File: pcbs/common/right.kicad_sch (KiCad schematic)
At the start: 88 parts

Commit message: upload of pcb
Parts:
- removed rC? (x2): 27p, Capacitor_SMD:C_0402_1005Metric, symbol Device:C_Small
- removed rC? (x9): 100n, Capacitor_SMD:C_0402_1005Metric, symbol Device:C_Small
- removed rC? (x3): 1u, Capacitor_SMD:C_0402_1005Metric, symbol Device:C_Small
- removed rC? (x2): 10u, Capacitor_SMD:C_0402_1005Metric, symbol Device:C_Small
- removed rD?: 1N4148WT, Diode_SMD:D_SOD-523, symbol Diode:1N4148WT
- removed rEXLED? (x2), rLED? (x21): YS-SK6812MINI-E, kbd_local:YS-SK6812MINI-E, symbol kbd_local:YS-SK6812MINI-E
- removed rEXSW? (x2): RotaryEncoder_Switch, kbd_local:keyswitch_cherrymx_hotswap_1u_rotary_encoder_ec12, symbol Device:RotaryEncoder_Switch
- removed rF?: BSMD0603-050-12V, Fuse:Fuse_0603_1608Metric, symbol Device:Fuse
- removed rJ?: TYPE-C-31-M-13C, kbd_local:TYPE-C-31-M-13C, symbol Connector:USB_C_Receptacle_USB2.0
- removed rJ?: Conn_01x03, Connector_PinHeader_2.54mm:PinHeader_1x03_P2.54mm_Vertical, symbol Connector_Generic:Conn_01x03
- removed rJP1: SolderJumper_2_Bridged, Jumper:SolderJumper-2_P1.3mm_Open_RoundedPad1.0x1.5mm, symbol Jumper:SolderJumper_2_Bridged
- removed rR? (x2): 5.1k, Resistor_SMD:R_0402_1005Metric, symbol Device:R_Small
- removed rR? (x2): 1k, Resistor_SMD:R_0402_1005Metric, symbol Device:R
- removed rR?: 10k, Resistor_SMD:R_0402_1005Metric, symbol Device:R
- removed rR? (x2): 27, Resistor_SMD:R_0402_1005Metric, symbol Device:R_Small
- removed rSMDSW? (x2): TS-1088R-02026, kbd_local:TS-1088R-02026, symbol Switch:SW_Push
- removed rU?: NCP1117LPST33T3G, Package_TO_SOT_SMD:SOT-223-3_TabPin2, symbol Regulator_Linear:NCP1117-3.3_SOT223
- removed rU?: TPD4E05U06DQAR, Package_SON:USON-10_2.5x1.0mm_P0.5mm, symbol Power_Protection:TPD4EUSB30
- removed rU?: W25Q128JVSIQ, Package_SO:SOIC-8_5.23x5.23mm_P1.27mm, symbol Memory_Flash:W25Q128JVS
- removed rU?: RP2040, Package_DFN_QFN:QFN-56-1EP_7x7mm_P0.4mm_EP3.2x3.2mm, symbol MCU_RaspberryPi:RP2040
- removed rY?: 12MHz 18pF, Crystal:Crystal_SMD_3225-4Pin_3.2x2.5mm, symbol Device:Crystal_GND24_Small
- removed rZD?: ESD5Z5V0C, Diode_SMD:D_SOD-523, symbol Diode:ESD5Zxx
- added D1, D2: WS2812B, LED_SMD:LED_WS2812B_PLCC4_5.0x5.0mm_P3.2mm, symbol LED:WS2812B
- added LED43, LED45, LED46, LED48, LED49, LED51, LED52, LED54, LED55, LED57, LED58, LED60, LED61, LED62, LED63: MX_SK6812MINI-E, PCM_marbastlib-mx:LED_MX_6028R, symbol PCM_marbastlib-mx:MX_SK6812MINI-E
- added LED44, LED47, LED50, LED53, LED56, LED59: MX_SK6812MINI-E, PCM_marbastlib-mx:LED_MX_6028R-ROT, symbol PCM_marbastlib-mx:MX_SK6812MINI-E
- added U1: rp2040, various:rp2040promicro, symbol PCM_marbastlib-promicroish:rp2040
- rSW? (x20): footprint kbd:keyswitch_cherrymx_hotswap_1u -> PCM_marbastlib-mx:SW_MX_HS_CPG151101S11_1u
- rSW?: footprint kbd:keyswitch_cherrymx_hotswap_1.5u -> PCM_marbastlib-mx:SW_MX_HS_CPG151101S11_1u
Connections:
- net +5VR: now also D1.1 (VDD), D2.1 (VDD), LED43.1 (VDD), LED44.1 (VDD), LED45.1 (VDD), LED46.1 (VDD), LED47.1 (VDD), LED48.1 (VDD), LED49.1 (VDD), LED50.1 (VDD), LED51.1 (VDD), LED52.1 (VDD), LED53.1 (VDD), LED54.1 (VDD), LED55.1 (VDD), LED56.1 (VDD), LED57.1 (VDD), LED58.1 (VDD), LED59.1 (VDD), LED60.1 (VDD), LED61.1 (VDD), LED62.1 (VDD), LED63.1 (VDD), U1.5v
- net GNDR: now also D1.3 (VSS), D2.3 (VSS), LED43.4 (VSS), LED44.4 (VSS), LED45.4 (VSS), LED46.4 (VSS), LED47.4 (VSS), LED48.4 (VSS), LED49.4 (VSS), LED50.4 (VSS), LED51.4 (VSS), LED52.4 (VSS), LED53.4 (VSS), LED54.4 (VSS), LED55.4 (VSS), LED56.4 (VSS), LED57.4 (VSS), LED58.4 (VSS), LED59.4 (VSS), LED60.4 (VSS), LED61.4 (VSS), LED62.4 (VSS), LED63.4 (VSS), U1.G (GND)
- net KEY1: now also U1.0 (GP0)
- net KEY10: now also U1.5 (GP5)
- net KEY11: now also U1.16 (GP16)
- net KEY12: now also U1.27 (GP27)
- net KEY13: now also U1.28 (GP28)
- net KEY14: now also U1.21 (GP21)
- net KEY15: now also U1.8 (GP8)
- net KEY16: now also U1.9 (GP9)
- net KEY17: now also U1.23 (GP23)
- net KEY18: now also U1.29 (GP29)
- net KEY19: now also U1.11 (GP11)
- net KEY2: now also U1.3 (GP3)
- net KEY20: now also U1.20 (GP20)
- net KEY21: now also U1.25 (GP25)
- net KEY3: now also U1.14 (GP14)
- net KEY4: now also U1.22 (GP22)
- net KEY5: now also U1.26 (GP26)
- net KEY6: now also U1.15 (GP15)
- net KEY7: now also U1.4 (GP4)
- net KEY8: now also U1.1 (GP1)
- net KEY9: now also U1.2 (GP2)
- net LED: now also D2.2 (DOUT), U1.10 (GP10)
- net RE1A: no longer rJ?.1 (Pin_1)
- net REB: no longer rJ?.2 (Pin_2)
- net RX: now also U1.13 (GP13)
- net TX: now also U1.12 (GP12)
- new net: LED58.2 (DOUT), LED59.3 (DIN)
- new net: LED55.2 (DOUT), LED58.3 (DIN)
- new net: D1.2 (DOUT), D2.4 (DIN)
- new net: D1.4 (DIN), LED43.3 (DIN)
- new net: LED53.3 (DIN), LED56.2 (DOUT)
- new net: LED56.3 (DIN), LED59.2 (DOUT)
- new net: LED54.2 (DOUT), LED57.3 (DIN)
- new net: LED51.2 (DOUT), LED54.3 (DIN)
- new net: LED50.3 (DIN), LED53.2 (DOUT)
- new net: LED52.2 (DOUT), LED55.3 (DIN)
- new net: LED61.2 (DOUT), LED62.3 (DIN)
- new net: LED60.2 (DOUT), LED61.3 (DIN)
- new net: LED48.2 (DOUT), LED51.3 (DIN)
- new net: LED45.2 (DOUT), LED48.3 (DIN)
- new net: LED57.2 (DOUT), LED60.3 (DIN)
- new net: LED62.2 (DOUT), LED63.3 (DIN)
- new net: LED47.3 (DIN), LED50.2 (DOUT)
- new net: LED43.2 (DOUT), LED46.3 (DIN)
- new net: LED44.3 (DIN), LED47.2 (DOUT)
- new net: LED49.2 (DOUT), LED52.3 (DIN)
- new net: LED44.2 (DOUT), LED45.3 (DIN)
- new net: LED46.2 (DOUT), LED49.3 (DIN)
- new net SCL: U1.7 (GP7), rJ?.2 (Pin_2)
- new net SDA: U1.6 (GP6), rJ?.1 (Pin_1)
- no-connect marks 3 -> 4
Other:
- note removed: "DEBUG"
- note removed: "Flash memory"
- note removed: "LEDs"
- note removed: "SPLIT_HAND_PIN"
- note removed: "USB ESD"
- note removed: "boot switch"
- note removed: "close to pin 44"
- note removed: "close to pin 45"

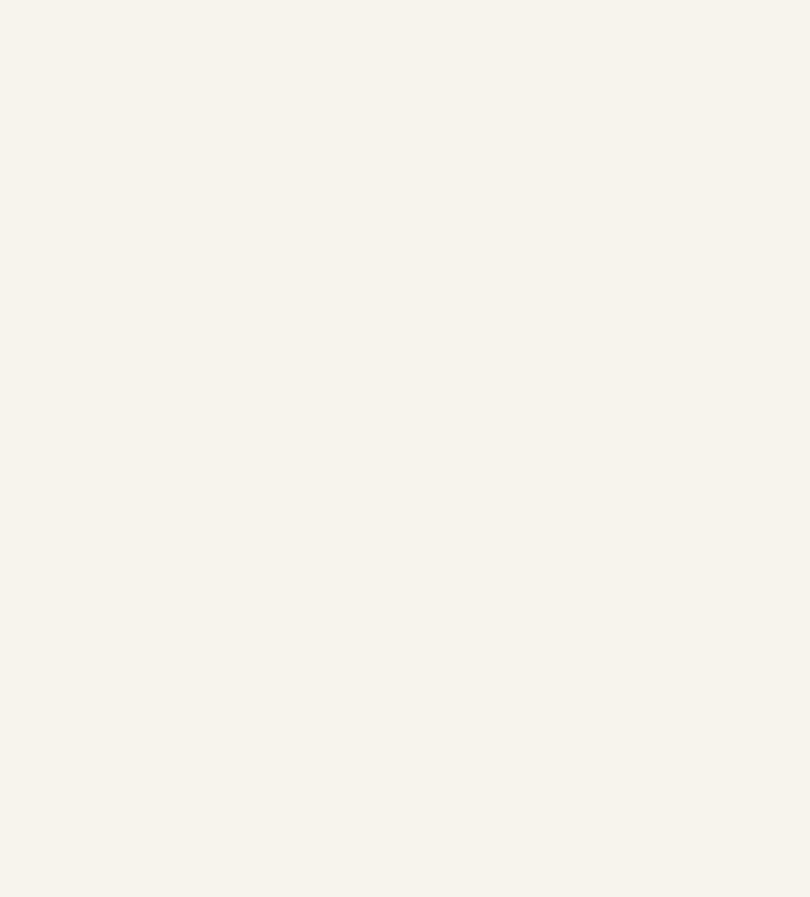
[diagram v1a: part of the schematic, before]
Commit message: split into left and right
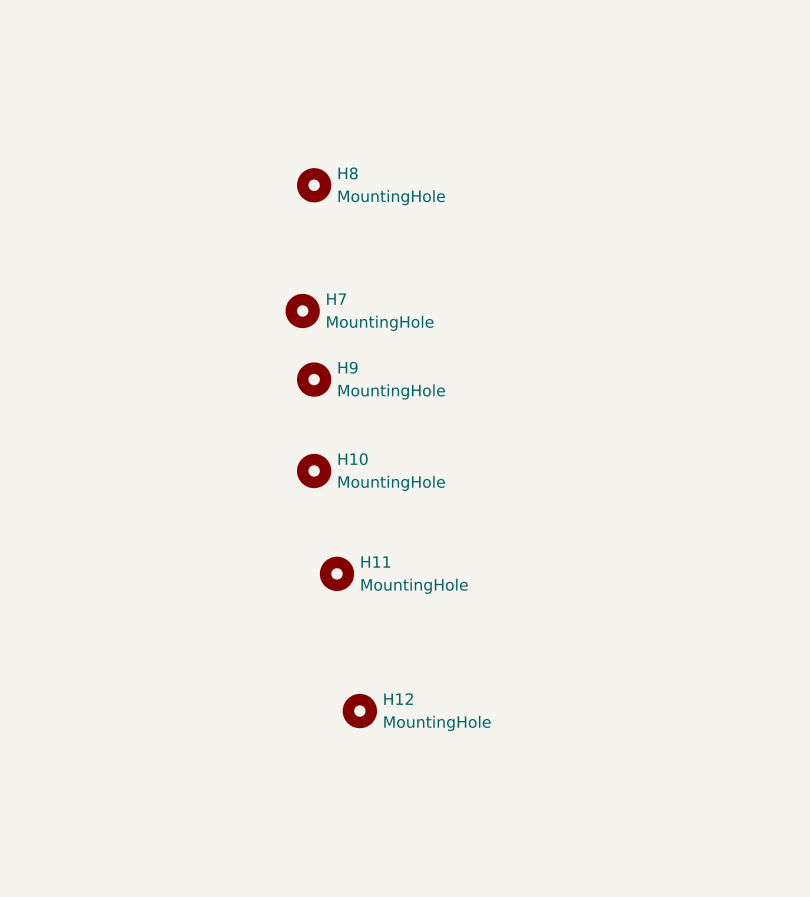
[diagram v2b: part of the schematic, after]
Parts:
- added H10, H11, H12, H7, H8, H9: MountingHole, MountingHole:MountingHole_2.2mm_M2, symbol Mechanical:MountingHole

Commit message: added zip files for prod
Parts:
- removed rBT1, rBT2, rBT3, rBT4: Breakaway Tabs, kbd_local:Breakaway_Tabs, symbol Mechanical:MountingHole
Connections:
- no-connect marks 4 -> 2
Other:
- note removed: "LDO"
- note removed: "MCU RP2040"
- note removed: "POWER"
- note removed: "VBUS ESD"
- moved on the sheet: D1, D2, LED43, LED44, LED45, LED46, LED47, LED48, LED49, LED50, LED51, LED52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
